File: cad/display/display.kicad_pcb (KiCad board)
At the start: 2 copper layers, 24 parts, among them P101 CONN_5X2, Q101 MOS_P, Q102 MOS_P, Q103 MOS_P, Q104 MOS_P, Q105 MOS_P, U101 CD74HC4017E, U102 74HC04, U103 LDS-A812RI, U104 LDS-A812RI, U105 LDS-A812RI, U106 LDS-A812RI, U107 LDS-A812RI, U108 TLC5916

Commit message: Committing the real v2 display layout
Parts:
- removed Q101, Q102, Q103, Q104, Q105: MOS_P, SOT23
- added 1pin_mech: VAL**, 1pin_mech, F.Cu at (246.8, 63.5)
- added Q1: 2N5461, TO92-123, F.Cu at (262.4, 67.3)
- added Q2: 2N5461, TO92-123, F.Cu at (284.5, 67.3)
- added Q3: 2N5461, TO92-123, F.Cu at (306.6, 67.3)
- added Q4: 2N5461, TO92-123, F.Cu at (328.7, 67.3)
- added Q5: 2N5461, TO92-123, F.Cu at (350.8, 67.3)
- C101, C102, C103, C104, P101, R101, R102, R103, R104, R105, R106: moved to B.Cu
- moved R105 196.6 mm to (354.6, 69.5)
- moved U107 189.5 mm to (341.9, 86.4)
- moved C101 183.8 mm to (325.8, 108.3), turned to 270 degrees
- moved U106 181.4 mm to (319.8, 86.4)
- moved P101 174.7 mm to (375.2, 87.1), turned to 270 degrees
- moved R106 172.4 mm to (362.5, 91.8)
- moved C104 172.0 mm to (362.5, 95.2), turned to 180 degrees
- moved C102 160.2 mm to (328.8, 108.3), turned to 270 degrees
- moved C103 159.3 mm to (362.5, 98.9), turned to 180 degrees
- moved R104 154.3 mm to (332.0, 69.7)
- moved R103 137.8 mm to (309.8, 69.5)
- moved U108 137.7 mm to (362.5, 86.4), turned to 90 degrees
- moved U103 135.1 mm to (253.5, 86.4)
- moved U105 133.5 mm to (297.7, 86.4)
- moved R102 126.5 mm to (287.7, 69.2)
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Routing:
- net +5V: track 0.00 -> 296.7 mm, vias 0 -> 2
- net N-0000032: track 0.00 -> 174.3 mm
- net /A: track 0.00 -> 140.0 mm
- net GND: track 0.00 -> 136.7 mm
- net /E: track 0.00 -> 124.9 mm, vias 0 -> 1
- net /D: track 0.00 -> 118.5 mm, vias 0 -> 1
- net /C: track 0.00 -> 115.1 mm, vias 0 -> 1
- net N-0000031: track 0.00 -> 114.5 mm, vias 0 -> 1
- net /F: track 0.00 -> 112.9 mm
- net /B: track 0.00 -> 110.4 mm
- net /RDP: track 0.00 -> 106.7 mm
- net /G: track 0.00 -> 102.8 mm
- net N-0000037: track 0.00 -> 74.1 mm, vias 0 -> 1
- net N-0000044: track 0.00 -> 65.2 mm
- net N-0000043: track 0.00 -> 63.4 mm
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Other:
- board outline added: 139.4 x 55.4 mm

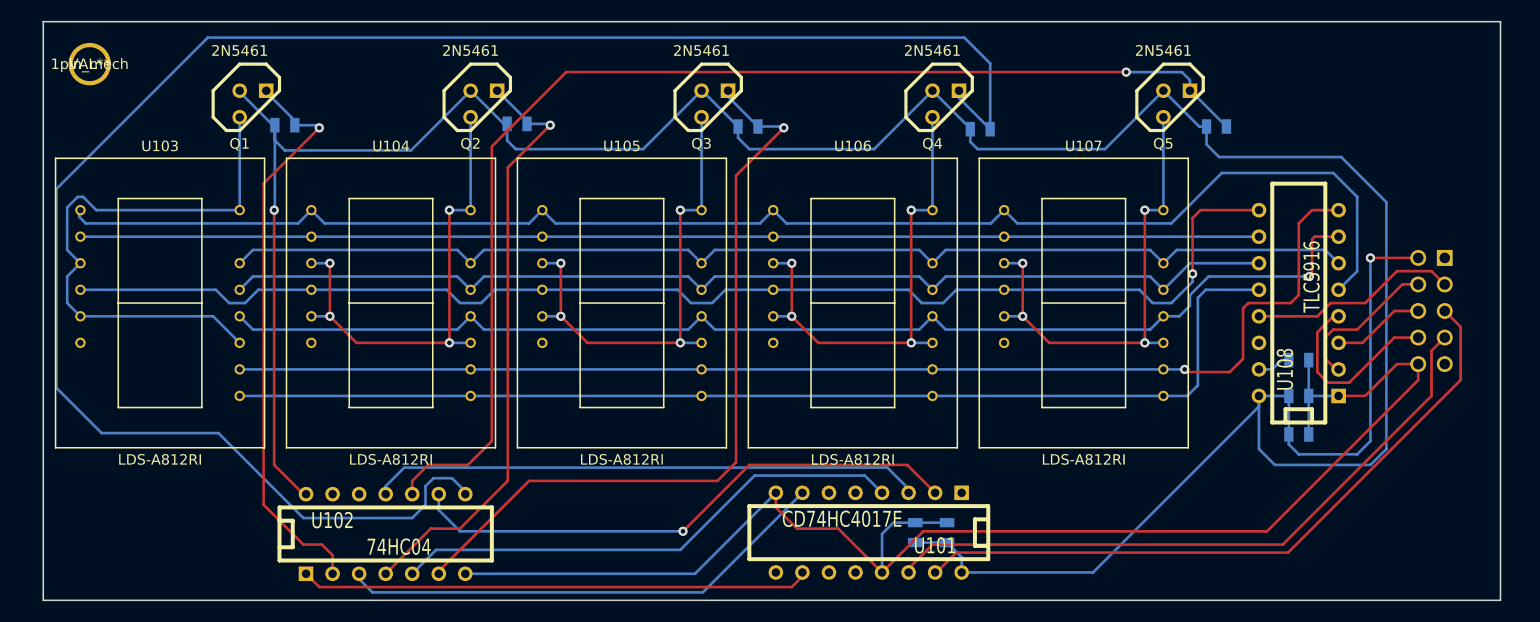
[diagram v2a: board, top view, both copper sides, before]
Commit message: Ground fills added, mounting holes too
Text also added. I think this is done.
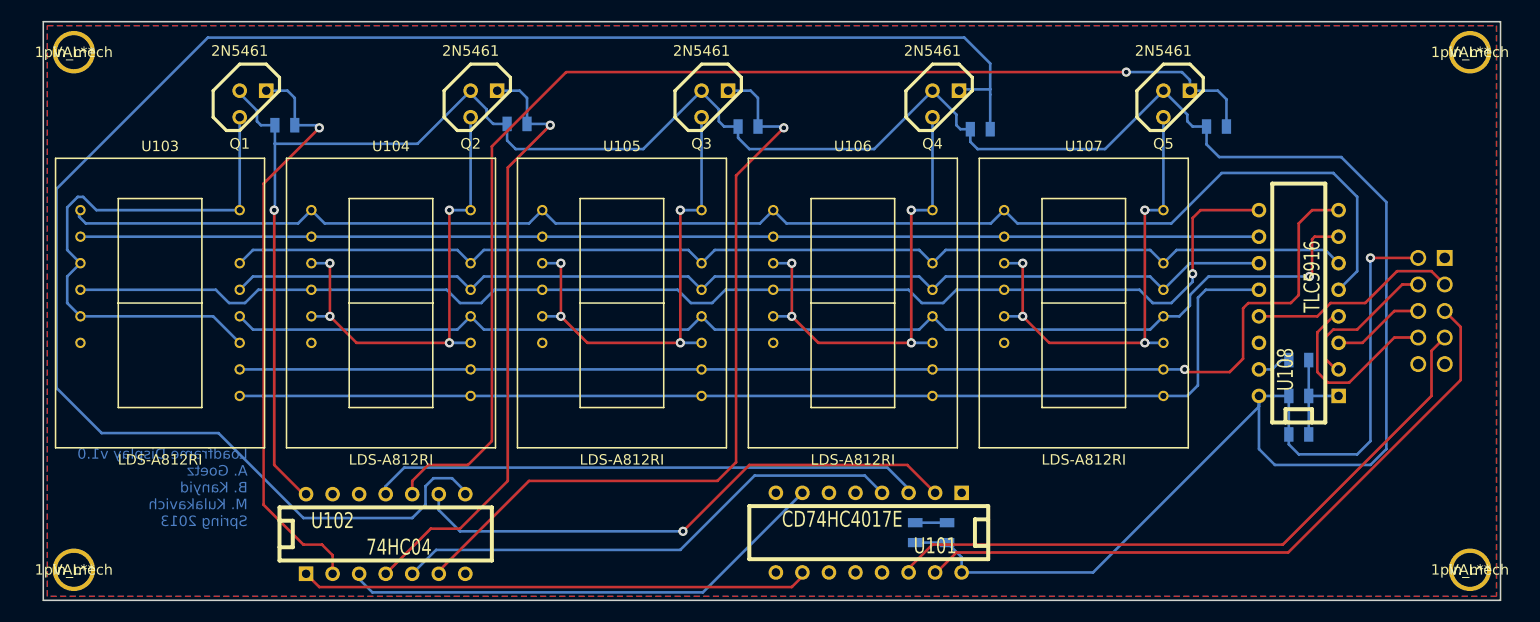
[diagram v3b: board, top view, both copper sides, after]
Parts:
- added 1pin_mech: VAL**, 1pin_mech, F.Cu at (378.8, 62.4)
- added 1pin_mech: VAL**, 1pin_mech, F.Cu at (378.8, 111.9)
- added 1pin_mech: VAL**, 1pin_mech, F.Cu at (245.2, 111.9)
- moved 1pin_mech 1.91 mm to (245.2, 62.4)
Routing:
- net GND: track 136.7 -> 13.0 mm
- net N-0000032: track 174.3 -> 172.4 mm
- net N-0000031: track 114.5 -> 116.2 mm
- net N-0000033: track 55.4 -> 56.7 mm
- net N-0000040: track 57.7 -> 59.0 mm
- net N-0000037: track 74.1 -> 75.3 mm
- net +5V: track 296.7 -> 297.6 mm
- added copper zone on B.Cu, net GND
- added copper zone on F.Cu, net GND
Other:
- board text added: "Loadframe Display v1.0 A. Goetz B. Kanyid M. Kulakavich Spring 2013"

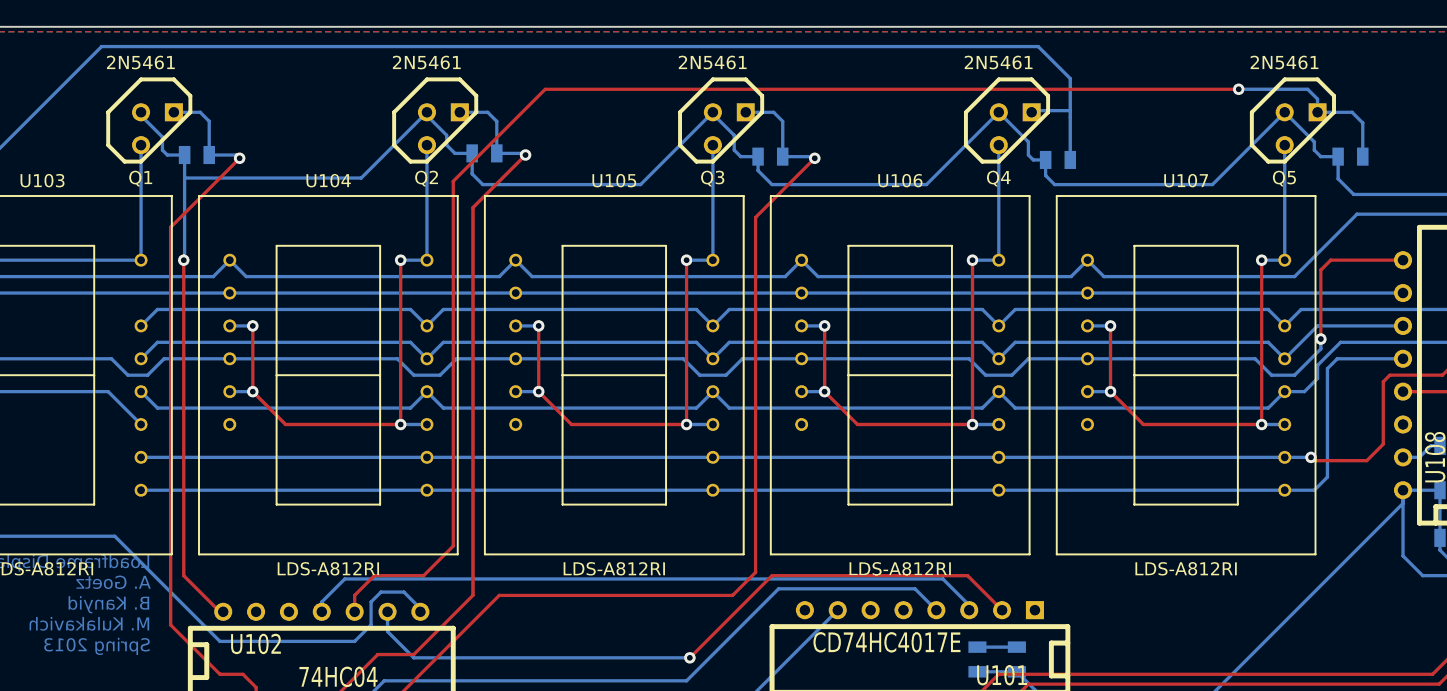
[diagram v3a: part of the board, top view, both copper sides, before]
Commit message: Rev2 of board w/ right transistors (PMOS SUCKS)
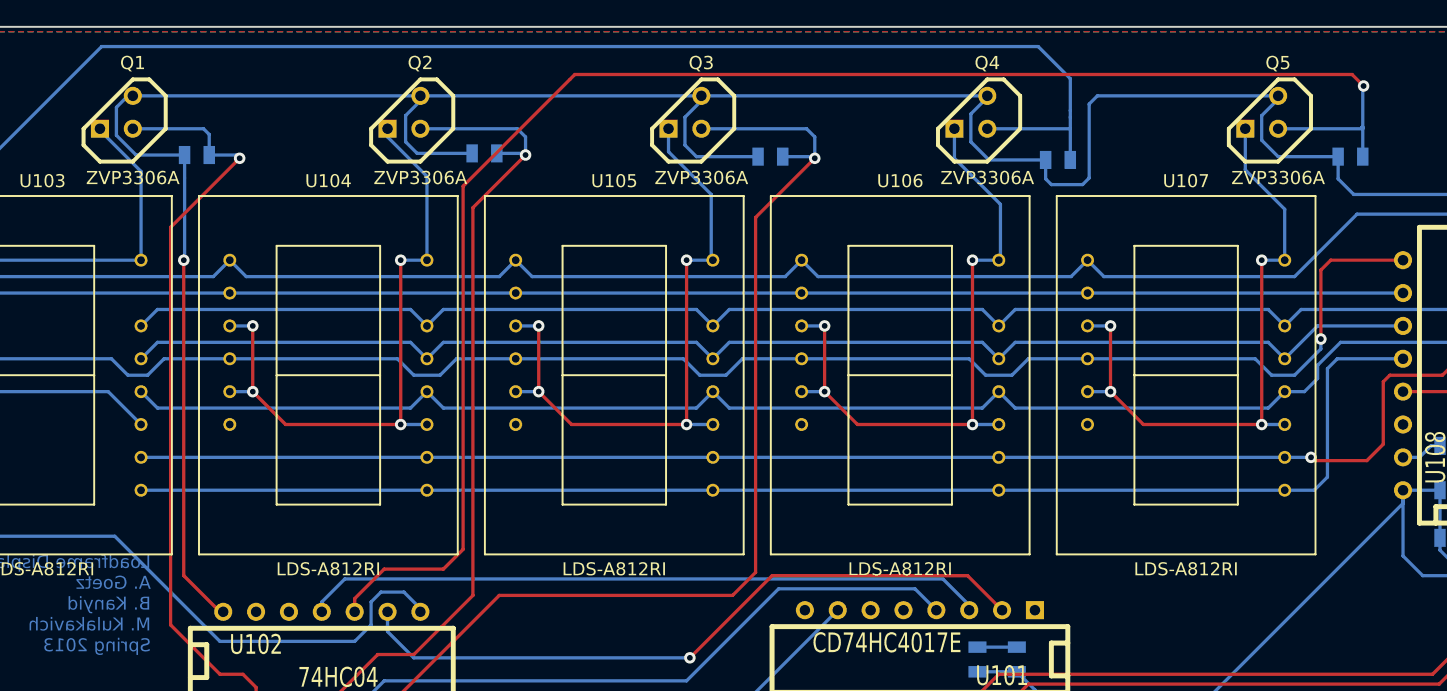
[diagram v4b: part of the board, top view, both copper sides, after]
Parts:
- Q1, Q2, Q3, Q4, Q5: value 2N5461 -> ZVP3306A
- moved Q3 3.66 mm to (303.1, 66.0), turned to 180 degrees
- moved Q4 3.66 mm to (325.2, 66.0), turned to 180 degrees
- moved Q1 3.42 mm to (259.2, 66.0), turned to 180 degrees
- moved Q2 3.30 mm to (281.4, 66.0), turned to 180 degrees
- moved Q5 3.30 mm to (347.7, 66.0), turned to 180 degrees
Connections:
- Q1 pad 1: N-0000014 -> +5V
- Q1 pad 2: +5V -> N-0000033
- Q1 pad 3: N-0000033 -> N-0000014
- Q2 pad 1: N-0000036 -> +5V
- Q2 pad 2: +5V -> N-0000040
- Q2 pad 3: N-0000040 -> N-0000036
- Q3 pad 1: N-0000038 -> +5V
- Q3 pad 2: +5V -> N-0000037
- Q3 pad 3: N-0000037 -> N-0000038
- Q4 pad 1: N-000004 -> +5V
- Q4 pad 2: +5V -> N-0000032
- Q4 pad 3: N-0000032 -> N-000004
- Q5 pad 1: N-0000041 -> +5V
- Q5 pad 2: +5V -> N-0000031
- Q5 pad 3: N-0000031 -> N-0000041
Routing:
- net +5V: track 297.6 -> 323.4 mm
- net N-0000031: track 116.2 -> 124.8 mm
- net N-0000037: track 75.3 -> 80.1 mm
- net N-0000040: track 59.0 -> 63.1 mm
- net N-0000032: track 172.4 -> 175.8 mm
- net N-000004: track 46.8 -> 49.6 mm
- net N-0000038: track 46.8 -> 49.5 mm
- net N-0000014: track 54.6 -> 57.2 mm
- net N-0000041: track 46.5 -> 49.1 mm
- net N-0000036: track 46.8 -> 49.3 mm
- net N-0000033: track 56.7 -> 58.8 mm

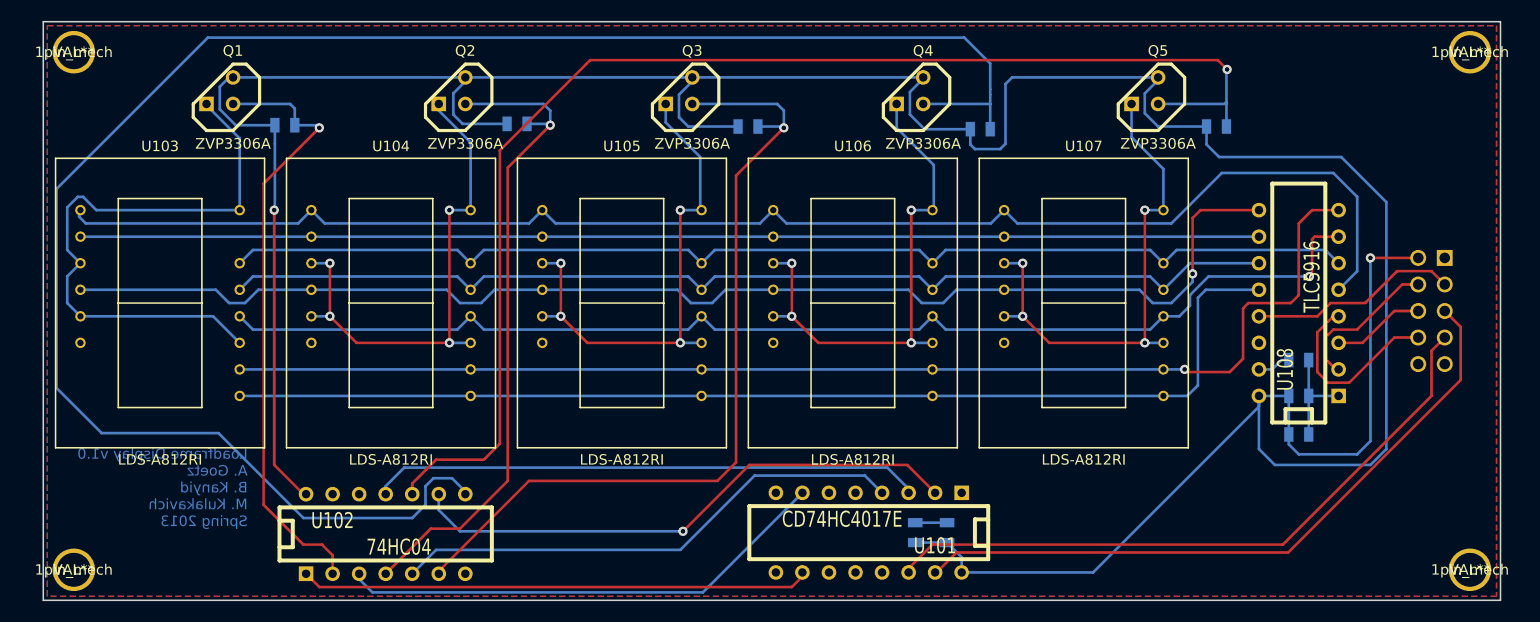
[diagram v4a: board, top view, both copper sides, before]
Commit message: PCB update (remove groundplane for EPL print)
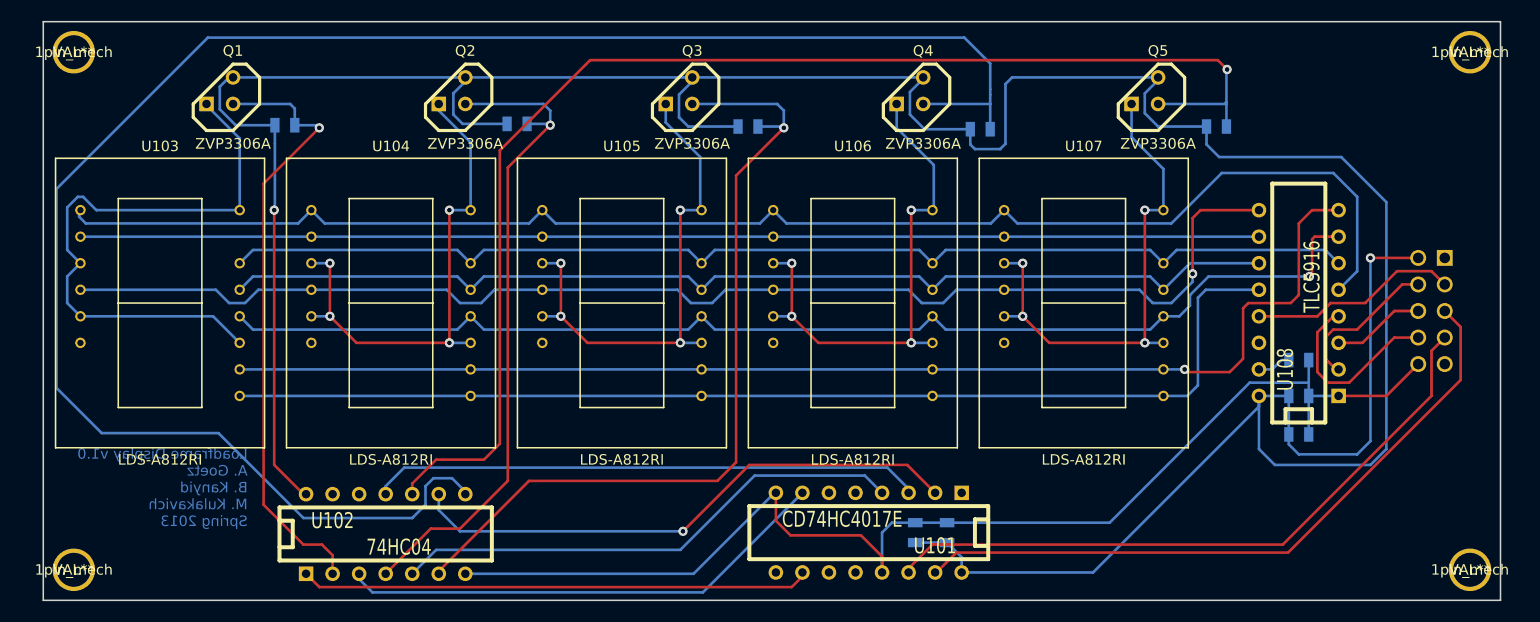
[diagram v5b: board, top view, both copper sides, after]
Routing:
- net GND: track 13.0 -> 118.3 mm
- removed copper zone on B.Cu, net GND
- removed copper zone on F.Cu, net GND
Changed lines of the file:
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@@
     (thickness 1.6)
     (drawings 5)
-    (tracks 413)
+    (tracks 432)
     (zones 0)
     (modules 28)
@@
     (visible_elements FFFFFFBF)
     (pcbplotparams
-      (layerselection 3178497)
+      (layerselection 268468225)
       (usegerberextensions true)
       (excludeedgelayer true)
@@
       (outputformat 1)
       (mirror false)
-      (drillshape 1)
+      (drillshape 0)
       (scaleselection 1)
-      (outputdirectory ""))
+      (outputdirectory gerbers/))
   )
   (net 0 "")
@@
   (segment (start 305.308 95.25) (end 283.21 95.25) (width 0.254) (layer B.Cu) (net 9))
   (segment (start 283.21 95.25) (end 261.112 95.25) (width 0.254) (layer B.Cu) (net 9))
+  (segment (start 366.268 95.25) (end 370.84 95.25) (width 0.254) (layer F.Cu) (net 10))
+  (segment (start 370.84 95.25) (end 373.888 92.202) (width 0.254) (layer F.Cu) (net 10))
+  (segment (start 328.803 107.3785) (end 344.3605 107.3785) (width 0.254) (layer B.Cu) (net 10))
+  (segment (start 357.759 93.98) (end 363.4105 93.98) (width 0.254) (layer B.Cu) (net 10))
+  (segment (start 344.3605 107.3785) (end 357.759 93.98) (width 0.254) (layer B.Cu) (net 10))
+  (segment (start 363.4105 93.98) (end 363.347 93.98) (width 0.254) (layer B.Cu) (net 10))
+  (segment (start 363.347 93.98) (end 363.4105 93.98) (width 0.254) (layer B.Cu) (net 10))
+  (segment (start 322.58 112.141) (end 322.58 108.331) (width 0.254) (layer B.Cu) (net 10))
+  (segment (start 323.5325 107.3785) (end 325.755 107.3785) (width 0.254) (layer B.Cu) (net 10))
+  (segment (start 322.58 108.331) (end 323.5325 107.3785) (width 0.254) (layer B.Cu) (net 10))
+  (segment (start 322.58 112.141) (end 322.58 110.617) (width 0.254) (layer F.Cu) (net 10))
+  (segment (start 312.42 107.188) (end 312.42 104.521) (width 0.254) (layer F.Cu) (net 10))
+  (segment (start 313.817 108.585) (end 312.42 107.188) (width 0.254) (layer F.Cu) (net 10))
+  (segment (start 320.548 108.585) (end 313.817 108.585) (width 0.254) (layer F.Cu) (net 10))
+  (segment (start 322.58 110.617) (end 320.548 108.585) (width 0.254) (layer F.Cu) (net 10))
+  (segment (start 312.42 104.521) (end 312.293 104.521) (width 0.254) (layer B.Cu) (net 10))
+  (segment (start 304.546 112.268) (end 282.702 112.268) (width 0.254) (layer B.Cu) (net 10))
+  (segment (start 312.293 104.521) (end 304.546 112.268) (width 0.254) (layer B.Cu) (net 10))
   (segment (start 325.755 107.3785) (end 328.803 107.3785) (width 0.254) (layer B.Cu) (net 10))
-  (segment (start 363.4105 91.821) (end 363.4105 95.25) (width 0.254) (layer B.Cu) (net 10))
+  (segment (start 363.4105 91.821) (end 363.4105 93.98) (width 0.254) (layer B.Cu) (net 10))
+  (segment (start 363.4105 93.98) (end 363.4105 95.25) (width 0.254) (layer B.Cu) (net 10))
   (segment (start 363.4105 95.25) (end 366.268 95.25) (width 0.254) (layer B.Cu) (net 10))
   (segment (start 363.4105 98.933) (end 363.4105 95.25) (width 0.254) (layer B.Cu) (net 10))
@@
   (segment (start 329.692 110.236) (end 361.442 110.236) (width 0.254) (layer F.Cu) (net 32))
   (segment (start 327.787 112.141) (end 329.692 110.236) (width 0.254) (layer F.Cu) (net 32))
-  (zone (net 10) (net_name GND) (layer F.Cu) (hatch edge 0.508)
-    (connect_pads (clearance 0.508))
-    (min_thickness 0.254)
-    (fill (arc_segments 16) (thermal_gap 0.508) (thermal_bridge_width 0.381))
-    (polygon
-      (pts
-        (xy 381.381 114.427) (xy 242.697 114.427) (xy 242.697 59.817) (xy 381.381 59.817)
-      )
-    )
-  )
-  (zone (net 10) (net_name GND) (layer B.Cu) (hatch edge 0.508)
-    (connect_pads (clearance 0.508))
-    (min_thickness 0.254)
-    (fill (arc_segments 16) (thermal_gap 0.508) (thermal_bridge_width 0.381))
-    (polygon
-      (pts
-        (xy 381.381 114.427) (xy 242.697 114.427) (xy 242.697 59.817) (xy 381.381 59.817)
-      )
-    )
-  )
 )

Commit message: Changed trace width to 20 mils. Had to move some things around
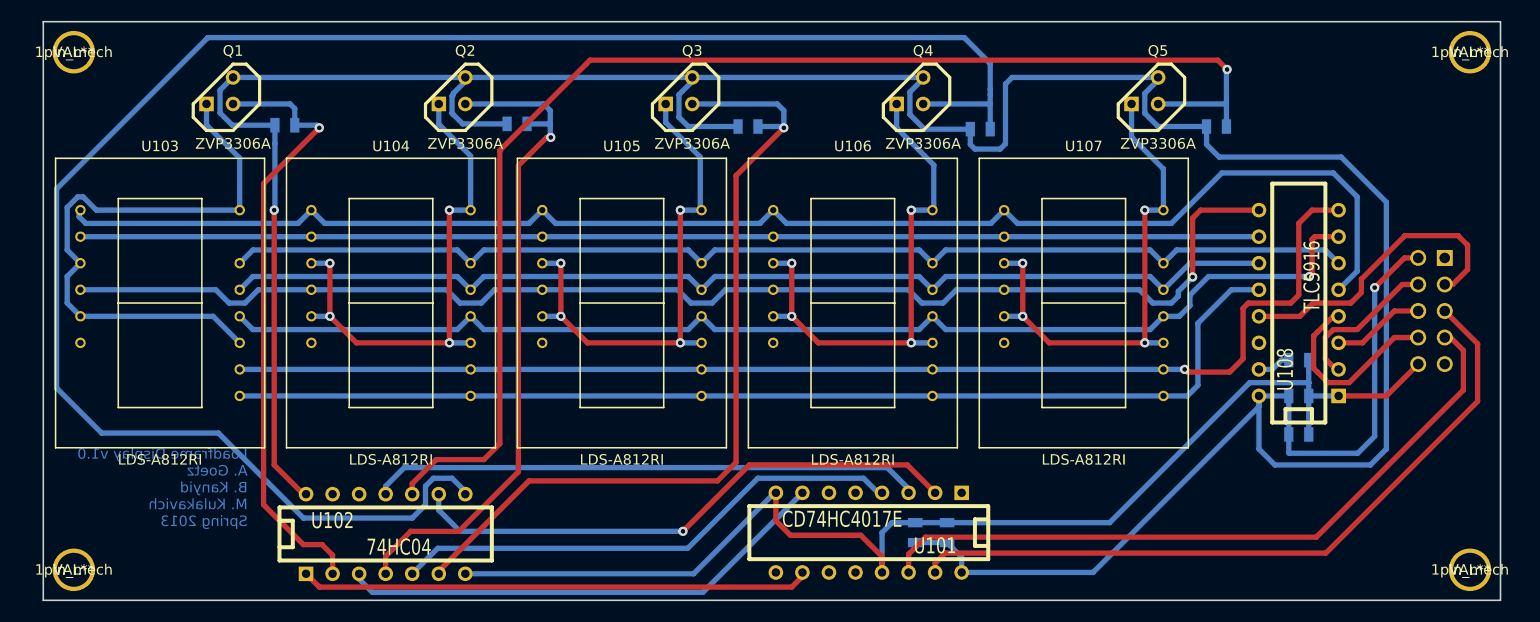
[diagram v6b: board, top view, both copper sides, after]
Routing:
- net N-0000026: track 20.1 -> 29.4 mm
- net N-0000044: track 65.2 -> 69.3 mm
- net N-0000043: track 63.4 -> 67.4 mm
- net +5V: track 323.4 -> 321.9 mm
- net /RDP: track 106.7 -> 105.2 mm
- net N-0000040: track 63.1 -> 64.5 mm
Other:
- net class Default: trace_width 0.254 -> 0.508
- rule trace_min: 0.254 -> 0.508
